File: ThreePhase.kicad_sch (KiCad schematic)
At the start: 19 parts, among them Q1 HYG025N06LS1C2, Q2 HYG025N06LS1C2, Q3 HYG025N06LS1C2, Q4 HYG025N06LS1C2, Q5 HYG025N06LS1C2, Q6 HYG025N06LS1C2

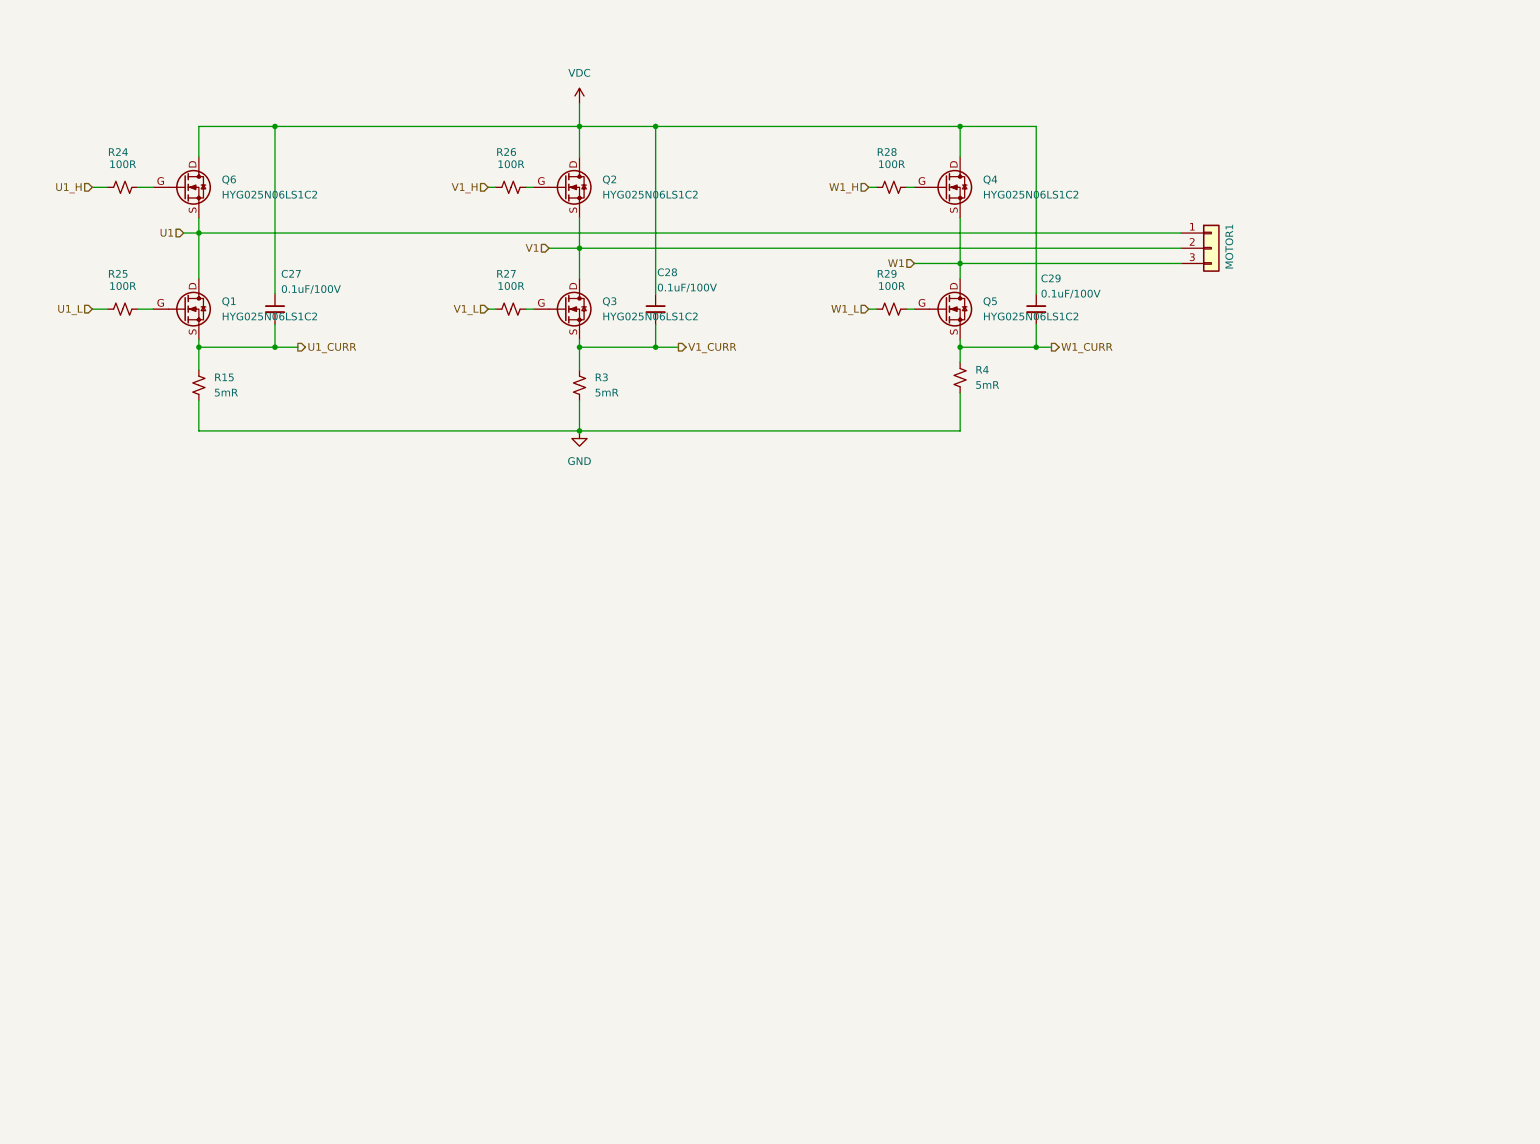
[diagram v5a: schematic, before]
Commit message: 三相桥基极增加回流路径,增加VDC的输入电容
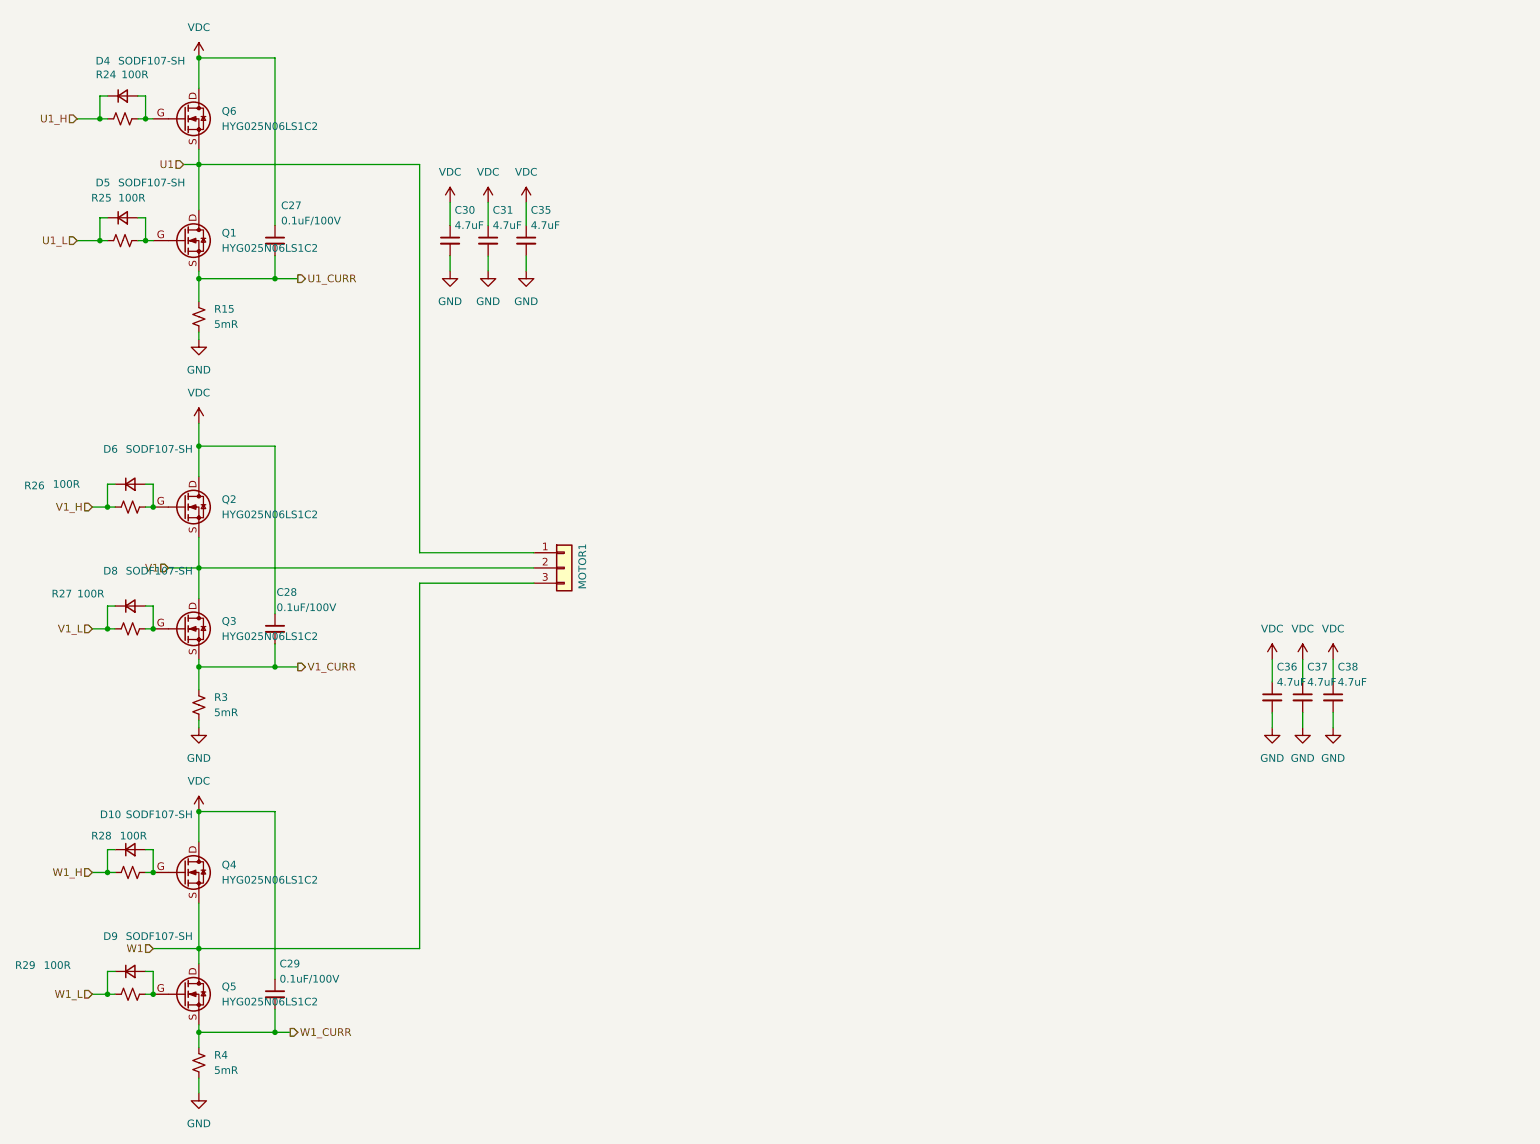
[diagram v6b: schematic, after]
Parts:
- added C30, C31, C35, C36, C37, C38: 4.7uF, Capacitor_SMD:C_1206_3216Metric, symbol Device:C_Small
- added D10, D4, D5, D6, D8, D9: SODF107-SH, Diode_SMD:D_SOD-123F, symbol Device:D_Small
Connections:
- net GND: now also C30.2, C31.2, C35.2, C36.2, C37.2, C38.2
- net U1_H: now also D4.1 (K)
- net U1_L: now also D5.1 (K)
- net V1_H: now also D6.1 (K)
- net V1_L: now also D8.1 (K)
- net VDC: now also C30.1, C31.1, C35.1, C36.1, C37.1, C38.1
- net W1_H: now also D10.1 (K)
- net W1_L: now also D9.1 (K)
- net at Q2.G, R26.2: now also D6.2 (A)
- net at Q5.G, R29.2: now also D9.2 (A)
- net at Q4.G, R28.2: now also D10.2 (A)
- net at Q6.G, R24.2: now also D4.2 (A)
- net at Q1.G, R25.2: now also D5.2 (A)
- net at Q3.G, R27.2: now also D8.2 (A)
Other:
- moved on the sheet: C27, C28, C29, MOTOR1, Q1, Q2, Q3, Q4, Q5, Q6, R15, R24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

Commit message: 优化原理图
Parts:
- added C27: 0.1uF/100V, Capacitor_SMD:C_0603_1608Metric, symbol Device:C_Small
- renumbered C27 to C20, C28 to C21, C29 to C22, C30 to C23, C36 to C24, C31 to C25, C37 to C26, C35 to C28, C38 to C29, D4 to D2, D5 to D3, D6 to D4, D8 to D5, D10 to D6, D9 to D7, Q6 to Q1, Q1 to Q2, Q2 to Q3, Q3 to Q4, Q4 to Q5, Q5 to Q6, R24 to R15, R25 to R16, R15 to R17, R26 to R18, R27 to R19, R3 to R20, R28 to R21, R29 to R22, R4 to R23
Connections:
- net GND: now also C27.1; no longer C23.2, C24.2, C25.2, C26.2, C28.2, C29.2, R17.2, R20.2, R23.2
- new net GNDPWR: C23.2, C24.2, C25.2, C26.2, C27.2, C28.2, C29.2, R17.2, R20.2, R23.2
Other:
- moved on the sheet: C21, C22, C23, C24, C25, C26, C28, C29, D4, D5, D6, D7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

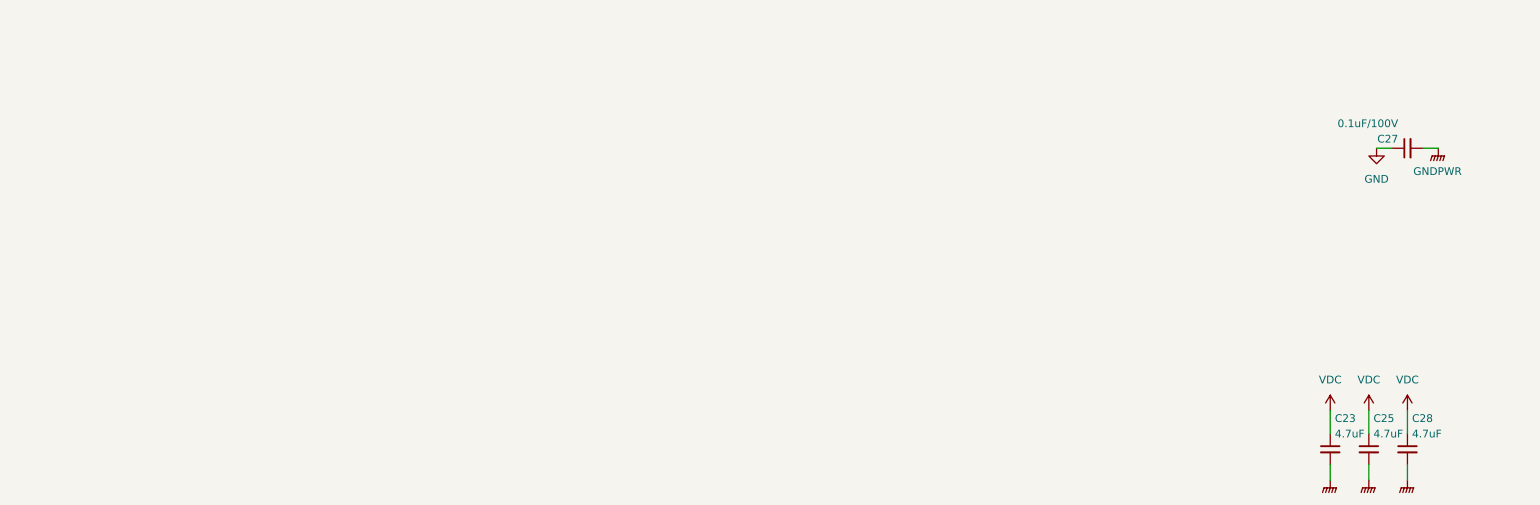
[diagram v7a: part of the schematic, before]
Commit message: 原理图增加motor2部分
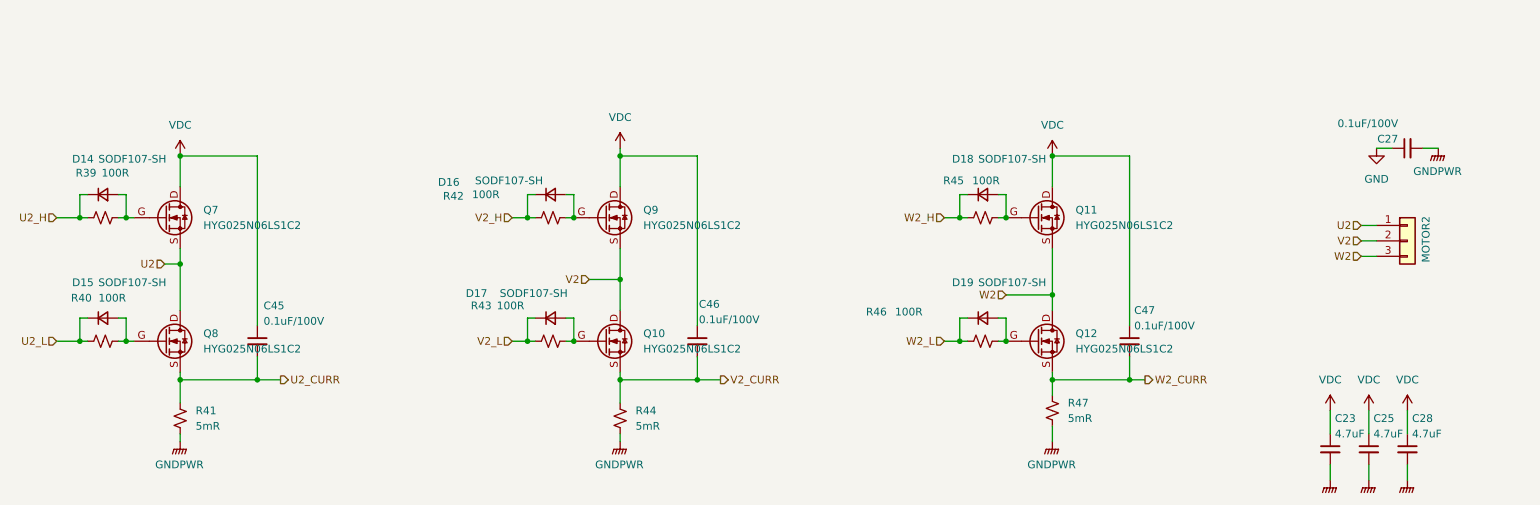
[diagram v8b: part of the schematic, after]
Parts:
- added C45, C46, C47: 0.1uF/100V, Capacitor_SMD:C_0603_1608Metric, symbol Device:C_Small
- added D14, D15, D16, D17, D18, D19: SODF107-SH, Diode_SMD:D_SOD-123F, symbol Device:D_Small
- added MOTOR2: Conn_01x03, footprints:MR30PW-FB_1x03_P3.50mm_Horizontal, symbol Connector_Generic:Conn_01x03
- added Q10, Q11, Q12, Q7, Q8, Q9: HYG025N06LS1C2, footprints:HYG025N06LS1C2-PDFN-8-1EP_6x5mm_P1.27mm_EP3x3mm, symbol User_Driver:NMOS_GDS
- added R39, R40, R42, R43, R45, R46: 100R, Resistor_SMD:R_0603_1608Metric, symbol Device:R_Small_US
- added R41, R44, R47: 5mR, Resistor_SMD:R_1206_3216Metric_Pad1.30x1.75mm_HandSolder, symbol Device:R_Small_US
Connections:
- net GNDPWR: now also R41.2, R44.2, R47.2
- net VDC: now also C45.1, C46.1, C47.1, Q11.D, Q7.D, Q9.D
- new net: D18.2 (A), Q11.G, R45.2
- new net: D17.2 (A), Q10.G, R43.2
- new net: D16.2 (A), Q9.G, R42.2
- new net: D19.2 (A), Q12.G, R46.2
- new net: D15.2 (A), Q8.G, R40.2
- new net: D14.2 (A), Q7.G, R39.2
- new net U2: MOTOR2.1 (Pin_1), Q7.S, Q8.D
- new net U2_CURR: C45.2, Q8.S, R41.1
- new net U2_H: D14.1 (K), R39.1
- new net U2_L: D15.1 (K), R40.1
- new net V2: MOTOR2.2 (Pin_2), Q10.D, Q9.S
- new net V2_CURR: C46.2, Q10.S, R44.1
- new net V2_H: D16.1 (K), R42.1
- new net V2_L: D17.1 (K), R43.1
- new net W2: MOTOR2.3 (Pin_3), Q11.S, Q12.D
- new net W2_CURR: C47.2, Q12.S, R47.1
- new net W2_H: D18.1 (K), R45.1
- new net W2_L: D19.1 (K), R46.1
